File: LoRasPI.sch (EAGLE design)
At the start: 10 parts, among them J1 JUMPER_1X30805

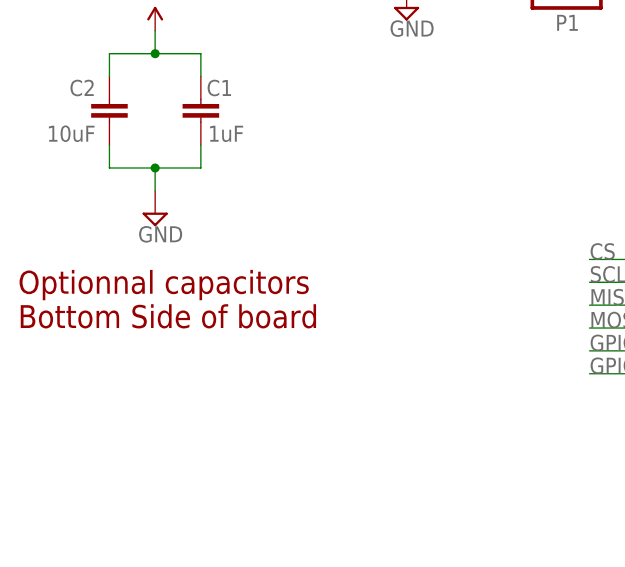
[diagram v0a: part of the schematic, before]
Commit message: small typo in 'Optionnal'
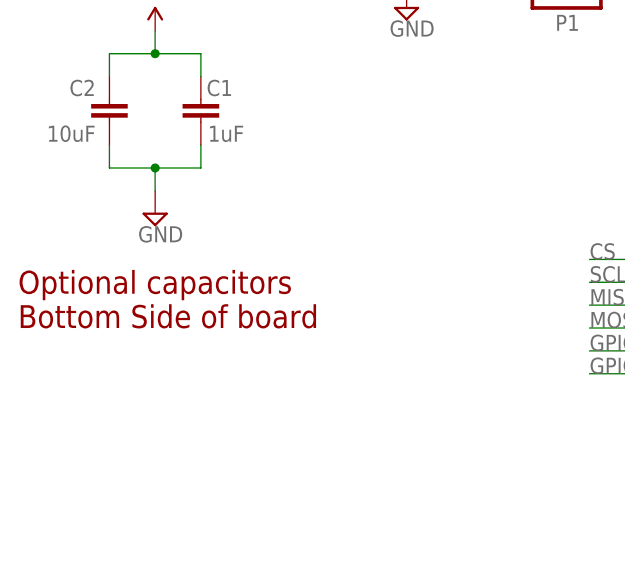
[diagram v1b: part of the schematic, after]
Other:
- note added: "Optional capacitors Bottom Side of board"
- note removed: "Optionnal capacitors Bottom Side of board"
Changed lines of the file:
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@@
 <text x="91.44" y="68.58" size="1.778" layer="95">CS</text>
 <text x="143.51" y="101.6" size="1.778" layer="95">CS</text>
-<text x="27.94" y="60.96" size="2.54" layer="94">Optionnal capacitors
+<text x="27.94" y="60.96" size="2.54" layer="94">Optional capacitors
 Bottom Side of board</text>
 </plain>

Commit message: Bump to V1.1
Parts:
- added D0: 1N4148, Seeed-Discrete:D-ESD-2P-CESD5V0D1
- added D3: TX/RX, _c2h:LED0805-LARGE
- added D4: CS, _c2h:LED0805-LARGE
- added R3: 10K, _c2h:RESISTOR0805-RES
- D1: value TX/RX -> 1N4148; device _c2h:LED0805-LARGE -> Seeed-Discrete:D-ESD-2P-CESD5V0D1
- D2: value CS -> 1N4148; device _c2h:LED0805-LARGE -> Seeed-Discrete:D-ESD-2P-CESD5V0D1
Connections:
- new net CS: HOPE-RF.SEL, J1.2, R2.2
- new net DIO0: D0.1, HOPE-RF.DIO0
- new net DIO1: D1.1, HOPE-RF.DIO1
- new net DIO2: D2.1, HOPE-RF.DIO2
- net 3V3: now also R3.1
- net CE0: no longer HOPE-RF.SEL, J1.2, R2.2
- net GND: now also D3.MINUS, D4.MINUS; no longer D1.MINUS, D2.MINUS
- net GPIO25: now also D0.2, D1.2, D2.2, R3.2; no longer HOPE-RF.DIO0
- net N$1: now also D3.PLUS; no longer D1.PLUS
- net N$2: now also D4.PLUS; no longer D2.PLUS
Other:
- note added: "Logic OR on DIO0/1/2 to be LIMC compatible but absolutly not mandatory since I made a software fix in LIMC"
- note added: "RFM69HCW"
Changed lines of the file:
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@@
 <setting verticaltext="up"/>
 </settings>
-<grid distance="100" unitdist="mil" unit="mil" style="dots" multiple="1" display="yes" altdistance="5" altunitdist="mil" altunit="mil"/>
+<grid distance="25" unitdist="mil" unit="mil" style="dots" multiple="1" display="yes" altdistance="5" altunitdist="mil" altunit="mil"/>
 <layers>
 <layer number="1" name="Top" color="4" fill="1" visible="no" active="no"/>
@@
 <part name="SUPPLY5" library="supply2" deviceset="GND" device=""/>
 <part name="R1" library="_c2h" deviceset="RESISTOR" device="0805-RES" value="390"/>
-<part name="D1" library="_c2h" deviceset="LED" device="0805-LARGE" value="TX/RX"/>
+<part name="D3" library="_c2h" deviceset="LED" device="0805-LARGE" value="TX/RX"/>
 <part name="SUPPLY6" library="supply2" deviceset="GND" device=""/>
-<part name="D2" library="_c2h" deviceset="LED" device="0805-LARGE" value="CS"/>
+<part name="D4" library="_c2h" deviceset="LED" device="0805-LARGE" value="CS"/>
 <part name="R2" library="_c2h" deviceset="RESISTOR" device="0805-RES" value="390"/>
 <part name="SUPPLY7" library="supply2" deviceset="GND" device=""/>
@@
 <part name="NAME" library="SparkFun-Aesthetics" deviceset="FRAME-A4L" device="" value="Value">
 <attribute name="CNAME" value="Lora Raspberry PI Gateway / Node"/>
-<attribute name="CREVISION" value="1.0"/>
+<attribute name="CREVISION" value="1.1"/>
 <attribute name="DESIGNER" value="Charles-Henri Hallard"/>
 </part>
+<part name="D0" library="Seeed-Discrete" deviceset="D-ESD-2P" device="-CESD5V0D1" value="1N4148"/>
+<part name="D1" library="Seeed-Discrete" deviceset="D-ESD-2P" device="-CESD5V0D1" value="1N4148"/>
+<part name="D2" library="Seeed-Discrete" deviceset="D-ESD-2P" device="-CESD5V0D1" value="1N4148"/>
+<part name="R3" library="_c2h" deviceset="RESISTOR" device="0805-RES" value="10K"/>
+<part name="P+4" library="_c2h" deviceset="3V3" device=""/>
 </parts>
 <sheets>
@@
 <text x="27.94" y="60.96" size="2.54" layer="94">Optional capacitors
 Bottom Side of board</text>
+<text x="114.3" y="68.58" size="1.6764" layer="94">RFM69HCW</text>
+<text x="31.115" y="15.875" size="2.54" layer="94">Logic OR on DIO0/1/2 to be
+LIMC compatible but absolutly
+not mandatory since I made
+a software fix in LIMC</text>
 </plain>
 <instances>
@@
 <attribute name="VALUE" x="156.21" y="109.982" size="1.778" layer="96" rot="R180"/>
 </instance>
-<instance part="D1" gate="G$1" x="167.64" y="111.76" smashed="yes" rot="R180">
+<instance part="D3" gate="G$1" x="167.64" y="111.76" smashed="yes" rot="R180">
 <attribute name="NAME" x="169.545" y="108.8136" size="1.778" layer="95"/>
 <attribute name="VALUE" x="162.56" y="114.173" size="1.778" layer="96"/>
 </instance>
 <instance part="SUPPLY6" gate="GND" x="176.53" y="111.76" rot="R90"/>
-<instance part="D2" gate="G$1" x="167.64" y="101.6" smashed="yes" rot="R180">
+<instance part="D4" gate="G$1" x="167.64" y="101.6" smashed="yes" rot="R180">
 <attribute name="NAME" x="169.545" y="98.6536" size="1.778" layer="95"/>
 <attribute name="VALUE" x="165.1" y="104.013" size="1.778" layer="96"/>
@@
 <attribute name="CREVISION" x="210.79" y="-17.88" size="2.54" layer="94" font="vector"/>
 </instance>
+<instance part="D0" gate="G$1" x="46.355" y="43.815" smashed="yes"/>
+<instance part="D1" gate="G$1" x="46.355" y="38.735" smashed="yes"/>
+<instance part="D2" gate="G$1" x="46.355" y="33.655" smashed="yes"/>
+<instance part="R3" gate="G$1" x="67.945" y="46.355" smashed="yes" rot="R270">
+<attribute name="NAME" x="64.3636" y="47.625" size="1.778" layer="95" rot="R270"/>
+<attribute name="VALUE" x="69.723" y="48.895" size="1.778" layer="96" rot="R270"/>
+</instance>
+<instance part="P+4" gate="3V3" x="67.945" y="54.61"/>
 </instances>
 <busses>
@@
 </segment>
 <segment>
-<pinref part="HOPE-RF" gate="G$1" pin="DIO0"/>
-<wire x1="104.14" y1="55.88" x2="91.44" y2="55.88" width="0.1524" layer="91"/>
-<label x="91.44" y="55.88" size="1.778" layer="95"/>
+<wire x1="52.705" y1="43.815" x2="52.705" y2="38.735" width="0.1524" layer="91"/>
+<wire x1="52.705" y1="38.735" x2="52.705" y2="33.655" width="0.1524" layer="91"/>
+<wire x1="52.705" y1="33.655" x2="48.895" y2="33.655" width="0.1524" layer="91"/>
+<pinref part="D0" gate="G$1" pin="2"/>
+<wire x1="48.895" y1="43.815" x2="52.705" y2="43.815" width="0.1524" layer="91"/>
+<pinref part="D1" gate="G$1" pin="2"/>
+<wire x1="48.895" y1="38.735" x2="52.705" y2="38.735" width="0.1524" layer="91"/>
+<pinref part="D2" gate="G$1" pin="2"/>
+<wire x1="52.705" y1="38.735" x2="67.945" y2="38.735" width="0.1524" layer="91"/>
+<junction x="52.705" y="38.735"/>
+<label x="70.485" y="38.735" size="1.778" layer="95"/>
+<pinref part="R3" gate="G$1" pin="2"/>
+<wire x1="67.945" y1="38.735" x2="81.28" y2="38.735" width="0.1524" layer="91"/>
+<wire x1="67.945" y1="41.275" x2="67.945" y2="38.735" width="0.1524" layer="91"/>
+<junction x="67.945" y="38.735"/>
 </segment>
 </net>
@@
 <segment>
 <pinref part="SUPPLY6" gate="GND" pin="GND"/>
-<pinref part="D1" gate="G$1" pin="MINUS"/>
+<pinref part="D3" gate="G$1" pin="MINUS"/>
 <wire x1="173.99" y1="111.76" x2="170.18" y2="111.76" width="0.1524" layer="91"/>
 </segment>
 <segment>
-<pinref part="D2" gate="G$1" pin="MINUS"/>
+<pinref part="D4" gate="G$1" pin="MINUS"/>
 <pinref part="SUPPLY7" gate="GND" pin="GND"/>
 <wire x1="170.18" y1="101.6" x2="173.99" y2="101.6" width="0.1524" layer="91"/>
@@
 <pinref part="P+3" gate="3V3" pin="3V3"/>
 </segment>
+<segment>
+<pinref part="R3" gate="G$1" pin="1"/>
+<pinref part="P+4" gate="3V3" pin="3V3"/>
+<wire x1="67.945" y1="54.61" x2="67.945" y2="51.435" width="0.1524" layer="91"/>
+</segment>
 </net>
 <net name="CE1" class="0">
@@
 <net name="N$1" class="0">
 <segment>
-<pinref part="D1" gate="G$1" pin="PLUS"/>
+<pinref part="D3" gate="G$1" pin="PLUS"/>
 <pinref part="R1" gate="G$1" pin="1"/>
 <wire x1="162.56" y1="111.76" x2="160.02" y2="111.76" width="0.1524" layer="91"/>
@@
 <net name="N$2" class="0">
 <segment>
-<pinref part="D2" gate="G$1" pin="PLUS"/>
+<pinref part="D4" gate="G$1" pin="PLUS"/>
 <wire x1="162.56" y1="101.6" x2="160.02" y2="101.6" width="0.1524" layer="91"/>
 <pinref part="R2" gate="G$1" pin="1"/>
@@
 <net name="CE0" class="0">
 <segment>
-<pinref part="R2" gate="G$1" pin="2"/>
-<pinref part="J1" gate="G$1" pin="2"/>
-<wire x1="127" y1="101.6" x2="149.86" y2="101.6" width="0.1524" layer="91"/>
 <pinref part="U$2" gate="G$1" pin="24"/>
 <wire x1="96.52" y1="101.6" x2="120.65" y2="101.6" width="0.1524" layer="91"/>
@@
 <pinref part="J1" gate="G$1" pin="1"/>
 <wire x1="120.65" y1="104.14" x2="127" y2="104.14" width="0.1524" layer="91"/>
-<wire x1="127" y1="101.6" x2="120.65" y2="101.6" width="0.1524" layer="91"/>
-<junction x="120.65" y="101.6"/>
-<junction x="127" y="101.6"/>
-</segment>
+</segment>
+</net>
+<net name="DIO2" class="0">
+<segment>
+<pinref part="D2" gate="G$1" pin="1"/>
+<wire x1="42.545" y1="33.655" x2="34.925" y2="33.655" width="0.1524" layer="91"/>
+<label x="37.465" y="33.655" size="1.778" layer="95"/>
+</segment>
+<segment>
+<pinref part="HOPE-RF" gate="G$1" pin="DIO2"/>
+<wire x1="129.54" y1="58.42" x2="140.97" y2="58.42" width="0.1524" layer="91"/>
+<label x="132.08" y="58.42" size="1.778" layer="95"/>
+</segment>
+</net>
+<net name="DIO1" class="0">
+<segment>
+<pinref part="D1" gate="G$1" pin="1"/>
+<wire x1="42.545" y1="38.735" x2="34.925" y2="38.735" width="0.1524" layer="91"/>
+<label x="37.465" y="38.735" size="1.778" layer="95"/>
+</segment>
+<segment>
+<pinref part="HOPE-RF" gate="G$1" pin="DIO1"/>
+<wire x1="104.14" y1="53.34" x2="91.44" y2="53.34" width="0.1524" layer="91"/>
+<label x="91.44" y="53.34" size="1.778" layer="95"/>
+</segment>
+</net>
+<net name="DIO0" class="0">
+<segment>
+<pinref part="D0" gate="G$1" pin="1"/>
+<wire x1="42.545" y1="43.815" x2="34.925" y2="43.815" width="0.1524" layer="91"/>
+<label x="37.465" y="43.815" size="1.778" layer="95"/>
+</segment>
+<segment>
+<pinref part="HOPE-RF" gate="G$1" pin="DIO0"/>
+<wire x1="104.14" y1="55.88" x2="91.44" y2="55.88" width="0.1524" layer="91"/>
+<label x="91.44" y="55.88" size="1.778" layer="95"/>
+</segment>
+</net>
+<net name="CS" class="0">
 <segment>
 <pinref part="HOPE-RF" gate="G$1" pin="SEL"/>
 <wire x1="104.14" y1="68.58" x2="91.44" y2="68.58" width="0.1524" layer="91"/>
 </segment>
-</net>
+<segment>
+<pinref part="R2" gate="G$1" pin="2"/>
+<pinref part="J1" gate="G$1" pin="2"/>
+<wire x1="127" y1="101.6" x2="149.86" y2="101.6" width="0.1524" layer="91"/>
+</segment>
+</net>

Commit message: Version 1.2
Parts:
- D4: value CS -> LED
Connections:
- net 3V3: no longer R3.1
- net CS: no longer J1.2, R2.2
- net GND: now also R3.1
- net GPIO24: now also R2.2; no longer HOPE-RF.DIO5
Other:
- note added: "DIO0"
- note added: "Logic OR on DIO0/1/2 to be LMIC compatible but absolutly not mandatory since I made a software fix in LMIC"
- note added: "RST"
- note removed: "Logic OR on DIO0/1/2 to be LIMC compatible but absolutly not mandatory since I made a software fix in LIMC"
- moved on the sheet: R3
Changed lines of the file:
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@@
 <setting verticaltext="up"/>
 </settings>
-<grid distance="25" unitdist="mil" unit="mil" style="dots" multiple="1" display="yes" altdistance="5" altunitdist="mil" altunit="mil"/>
+<grid distance="50" unitdist="mil" unit="mil" style="dots" multiple="1" display="yes" altdistance="5" altunitdist="mil" altunit="mil"/>
 <layers>
 <layer number="1" name="Top" color="4" fill="1" visible="no" active="no"/>
@@
 <part name="D3" library="_c2h" deviceset="LED" device="0805-LARGE" value="TX/RX"/>
 <part name="SUPPLY6" library="supply2" deviceset="GND" device=""/>
-<part name="D4" library="_c2h" deviceset="LED" device="0805-LARGE" value="CS"/>
+<part name="D4" library="_c2h" deviceset="LED" device="0805-LARGE" value="LED"/>
 <part name="R2" library="_c2h" deviceset="RESISTOR" device="0805-RES" value="390"/>
 <part name="SUPPLY7" library="supply2" deviceset="GND" device=""/>
@@
 <part name="NAME" library="SparkFun-Aesthetics" deviceset="FRAME-A4L" device="" value="Value">
 <attribute name="CNAME" value="Lora Raspberry PI Gateway / Node"/>
-<attribute name="CREVISION" value="1.1"/>
+<attribute name="CREVISION" value="1.2"/>
 <attribute name="DESIGNER" value="Charles-Henri Hallard"/>
 </part>
@@
 <part name="D2" library="Seeed-Discrete" deviceset="D-ESD-2P" device="-CESD5V0D1" value="1N4148"/>
 <part name="R3" library="_c2h" deviceset="RESISTOR" device="0805-RES" value="10K"/>
-<part name="P+4" library="_c2h" deviceset="3V3" device=""/>
+<part name="SUPPLY8" library="supply2" deviceset="GND" device=""/>
 </parts>
 <sheets>
@@
 <text x="106.68" y="15.24" size="2.54" layer="94">See http://github/hallard/LoRasPI</text>
 <text x="91.44" y="68.58" size="1.778" layer="95">CS</text>
-<text x="143.51" y="101.6" size="1.778" layer="95">CS</text>
+<text x="138.43" y="101.6" size="1.778" layer="95">CS</text>
 <text x="27.94" y="60.96" size="2.54" layer="94">Optional capacitors
 Bottom Side of board</text>
 <text x="114.3" y="68.58" size="1.6764" layer="94">RFM69HCW</text>
-<text x="31.115" y="15.875" size="2.54" layer="94">Logic OR on DIO0/1/2 to be
-LIMC compatible but absolutly
+<text x="15.24" y="15.875" size="2.54" layer="94">Logic OR on DIO0/1/2 to be
+LMIC compatible but absolutly
 not mandatory since I made
-a software fix in LIMC</text>
+a software fix in LMIC</text>
+<text x="66.04" y="111.76" size="1.778" layer="94">RST</text>
+<text x="109.22" y="104.14" size="1.778" layer="94">DIO0</text>
 </plain>
 <instances>
@@
 <instance part="HOPE-RF" gate="G$1" x="116.84" y="63.5"/>
 <instance part="SUPPLY1" gate="GND" x="116.84" y="40.64"/>
-<instance part="SUPPLY2" gate="GND" x="111.76" y="106.68" rot="R90"/>
+<instance part="SUPPLY2" gate="GND" x="116.84" y="106.68" rot="R90"/>
 <instance part="SUPPLY3" gate="GND" x="71.12" y="96.52"/>
-<instance part="P+1" gate="3V3" x="63.5" y="109.22"/>
+<instance part="P+1" gate="3V3" x="53.34" y="109.22"/>
 <instance part="P+2" gate="3V3" x="116.84" y="78.74"/>
 <instance part="J$1" gate="1" x="157.48" y="63.5"/>
@@
 <instance part="D1" gate="G$1" x="46.355" y="38.735" smashed="yes"/>
 <instance part="D2" gate="G$1" x="46.355" y="33.655" smashed="yes"/>
-<instance part="R3" gate="G$1" x="67.945" y="46.355" smashed="yes" rot="R270">
-<attribute name="NAME" x="64.3636" y="47.625" size="1.778" layer="95" rot="R270"/>
-<attribute name="VALUE" x="69.723" y="48.895" size="1.778" layer="96" rot="R270"/>
-</instance>
-<instance part="P+4" gate="3V3" x="67.945" y="54.61"/>
+<instance part="R3" gate="G$1" x="67.945" y="31.75" smashed="yes" rot="R90">
+<attribute name="NAME" x="71.5264" y="30.48" size="1.778" layer="95" rot="R90"/>
+<attribute name="VALUE" x="66.167" y="29.21" size="1.778" layer="96" rot="R90"/>
+</instance>
+<instance part="SUPPLY8" gate="GND" x="67.945" y="22.86"/>
 </instances>
 <busses>
@@
 <segment>
 <pinref part="U$2" gate="G$1" pin="18"/>
-<wire x1="96.52" y1="109.22" x2="107.95" y2="109.22" width="0.1524" layer="91"/>
 <label x="99.06" y="109.22" size="1.778" layer="95"/>
-</segment>
-<segment>
-<pinref part="HOPE-RF" gate="G$1" pin="DIO5"/>
-<wire x1="129.54" y1="55.88" x2="140.97" y2="55.88" width="0.1524" layer="91"/>
-<label x="132.08" y="55.88" size="1.778" layer="95"/>
+<wire x1="96.52" y1="109.22" x2="147.32" y2="109.22" width="0.1524" layer="91"/>
+<wire x1="147.32" y1="109.22" x2="147.32" y2="101.6" width="0.1524" layer="91"/>
+<pinref part="R2" gate="G$1" pin="2"/>
+<wire x1="147.32" y1="101.6" x2="149.86" y2="101.6" width="0.1524" layer="91"/>
 </segment>
 </net>
@@
 <pinref part="R3" gate="G$1" pin="2"/>
 <wire x1="67.945" y1="38.735" x2="81.28" y2="38.735" width="0.1524" layer="91"/>
-<wire x1="67.945" y1="41.275" x2="67.945" y2="38.735" width="0.1524" layer="91"/>
+<wire x1="67.945" y1="36.83" x2="67.945" y2="38.735" width="0.1524" layer="91"/>
 <junction x="67.945" y="38.735"/>
 </segment>
@@
 <segment>
 <pinref part="U$2" gate="G$1" pin="20"/>
-<wire x1="96.52" y1="106.68" x2="109.22" y2="106.68" width="0.1524" layer="91"/>
+<wire x1="96.52" y1="106.68" x2="114.3" y2="106.68" width="0.1524" layer="91"/>
 <label x="99.06" y="106.68" size="1.778" layer="95"/>
 <pinref part="SUPPLY2" gate="GND" pin="GND"/>
@@
 <wire x1="170.18" y1="101.6" x2="173.99" y2="101.6" width="0.1524" layer="91"/>
 </segment>
+<segment>
+<pinref part="R3" gate="G$1" pin="1"/>
+<pinref part="SUPPLY8" gate="GND" pin="GND"/>
+<wire x1="67.945" y1="25.4" x2="67.945" y2="26.67" width="0.1524" layer="91"/>
+</segment>
 </net>
 <net name="3V3" class="0">
 <segment>
 <pinref part="U$2" gate="G$1" pin="17"/>
-<wire x1="81.28" y1="109.22" x2="63.5" y2="109.22" width="0.1524" layer="91"/>
+<wire x1="81.28" y1="109.22" x2="53.34" y2="109.22" width="0.1524" layer="91"/>
 <label x="71.12" y="109.22" size="1.778" layer="95"/>
 <pinref part="P+1" gate="3V3" pin="3V3"/>
@@
 <pinref part="P+3" gate="3V3" pin="3V3"/>
 </segment>
-<segment>
-<pinref part="R3" gate="G$1" pin="1"/>
-<pinref part="P+4" gate="3V3" pin="3V3"/>
-<wire x1="67.945" y1="54.61" x2="67.945" y2="51.435" width="0.1524" layer="91"/>
-</segment>
 </net>
 <net name="CE1" class="0">
@@
 </segment>
 <segment>
-<pinref part="R2" gate="G$1" pin="2"/>
-<pinref part="J1" gate="G$1" pin="2"/>
-<wire x1="127" y1="101.6" x2="149.86" y2="101.6" width="0.1524" layer="91"/>
-</segment>
-</net>
+<wire x1="127" y1="101.6" x2="140.97" y2="101.6" width="0.1524" layer="91"/>
+</segment>
+</net>

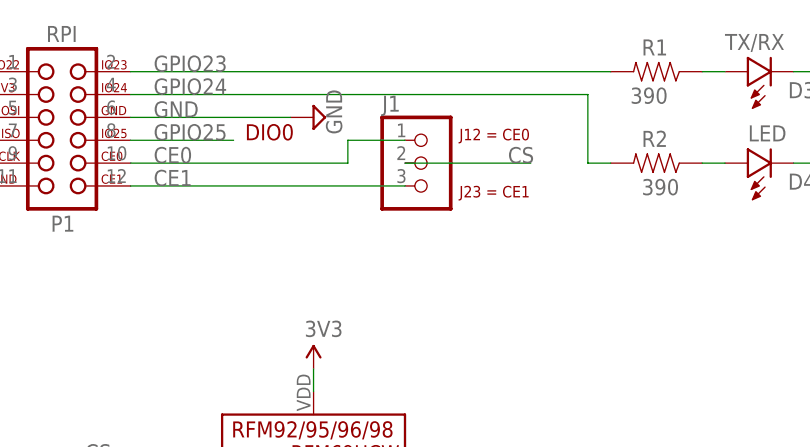
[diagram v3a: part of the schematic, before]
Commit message: V1.2a, fixed missing trace
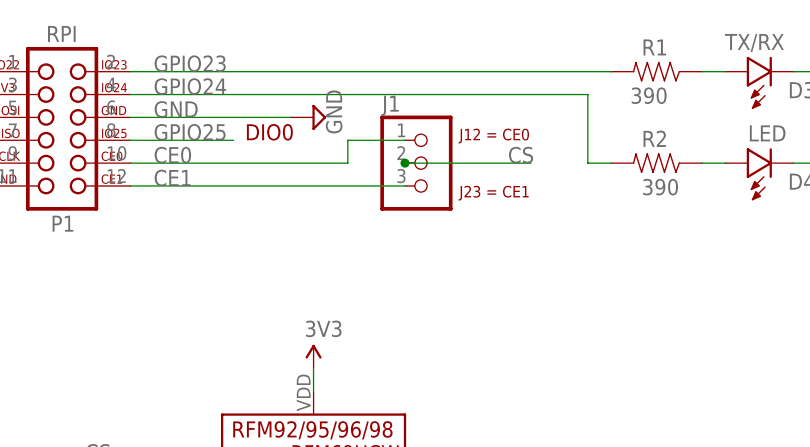
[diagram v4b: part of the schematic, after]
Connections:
- net CS: now also J1.2
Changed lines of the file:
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@@
 <setting verticaltext="up"/>
 </settings>
-<grid distance="50" unitdist="mil" unit="mil" style="dots" multiple="1" display="yes" altdistance="5" altunitdist="mil" altunit="mil"/>
+<grid distance="25" unitdist="mil" unit="mil" style="dots" multiple="1" display="yes" altdistance="5" altunitdist="mil" altunit="mil"/>
 <layers>
 <layer number="1" name="Top" color="4" fill="1" visible="no" active="no"/>
@@
 <part name="NAME" library="SparkFun-Aesthetics" deviceset="FRAME-A4L" device="" value="Value">
 <attribute name="CNAME" value="Lora Raspberry PI Gateway / Node"/>
-<attribute name="CREVISION" value="1.2"/>
+<attribute name="CREVISION" value="1.2a"/>
 <attribute name="DESIGNER" value="Charles-Henri Hallard"/>
 </part>
@@
 <segment>
 <wire x1="127" y1="101.6" x2="140.97" y2="101.6" width="0.1524" layer="91"/>
-</segment>
-</net>
+<pinref part="J1" gate="G$1" pin="2"/>
+<junction x="127" y="101.6"/>
+</segment>
+</net>
